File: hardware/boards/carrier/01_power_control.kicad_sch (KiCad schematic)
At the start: 15 parts, among them U1 STM32G031G6U6

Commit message: hardware: split carrier power controls and adopt SMBus
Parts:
- removed C11, C12: 100nF, Capacitor_SMD:C_0603_1608Metric, symbol Device:C
- removed C13: 4.7uF, Capacitor_SMD:C_0603_1608Metric, symbol Device:C
- removed LED1: WS2812B-2020-V6, LED_SMD:LED_WS2812B-2020_PLCC4_2.0x2.0mm, symbol LED:WS2812B-2020
- removed R24, R25, R26, R27: 2.2k, Resistor_SMD:R_0603_1608Metric, symbol Device:R
- removed R28: 10k, Resistor_SMD:R_0603_1608Metric, symbol Device:R
- removed R29: 100R, Resistor_SMD:R_0603_1608Metric, symbol Device:R
- removed TP1: SWDIO, TestPoint:TestPoint_Pad_D1.0mm, symbol Connector:TestPoint
- removed TP2: SWCLK, TestPoint:TestPoint_Pad_D1.0mm, symbol Connector:TestPoint
- removed TP3: NRST, TestPoint:TestPoint_Pad_D1.0mm, symbol Connector:TestPoint
- removed TP5: GND, TestPoint:TestPoint_Pad_D1.0mm, symbol Connector:TestPoint
- removed U1: STM32G031G6U6, Package_DFN_QFN:QFN-28_4x4mm_P0.5mm, symbol MCU_ST_STM32G0:STM32G031G6Ux
- added C1: 1uF 100V, Capacitor_SMD:C_1206_3216Metric, symbol Device:C
- added C10: 100nF, Capacitor_SMD:C_0603_1608Metric, symbol Device:C
- added C2: 680nF, Capacitor_SMD:C_0603_1608Metric, symbol Device:C
- added D1: SMCJ48A, Diode_SMD:D_SMC, symbol Device:D_Zener
- added MOD1: SW3538_140W_Module, mini-rack-power:SW3538_140W_Module, symbol mini-rack-power:SW3538_140W_Module
- added Q1: IPB020N10N5LF, Package_TO_SOT_SMD:TO-263-3_TabPin2, symbol Transistor_FET:Q_NMOS_GDS
- added Q2, Q3: 2N7002, Package_TO_SOT_SMD:SOT-23, symbol Transistor_FET:2N7002
- added R1: 6mR 1% 3W, Resistor_SMD:R_2512_6332Metric, symbol Device:R
- added R10: 100k, Resistor_SMD:R_0603_1608Metric, symbol Device:R
- added R11, R19: 10k, Resistor_SMD:R_0603_1608Metric, symbol Device:R
- added R17, R18: 10R, Resistor_SMD:R_0603_1608Metric, symbol Device:R
- added R2: 100R, Resistor_SMD:R_0603_1608Metric, symbol Device:R
- added R3: 36.0k 1%, Resistor_SMD:R_0603_1608Metric, symbol Device:R
- added R4, R6, R8: 110k 1%, Resistor_SMD:R_0603_1608Metric, symbol Device:R
- added R5: 18k 1%, Resistor_SMD:R_0603_1608Metric, symbol Device:R
- added R7: 5.1k 1%, Resistor_SMD:R_0603_1608Metric, symbol Device:R
- added R9: 36k 1%, Resistor_SMD:R_0603_1608Metric, symbol Device:R
- added U3: LMX5069MS, Package_SO:MSOP-10_3x3mm_P0.5mm, symbol Power_Management:LM5069MM-2
- added U4: INA237AIDGSR, Package_SO:TSSOP-10_3x3mm_P0.5mm, symbol Sensor_Energy:INA237
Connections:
- net +3V3: now also R11.1, R19.1, U4.6 (VS)
- net GND: now also C1.2, C2.2, D1.2 (A), MOD1.2 (GND), MOD1.4 (GND), Q2.2 (S), Q3.2 (S), R10.2, R3.2, R5.2, R7.2, R9.2, U3.5 (GND), U4.1 (A1), U4.2 (A0), U4.7 (GND)
- net INA_ALERT: now also R19.2, U4.3 (~{Alert})
- net PD_ENABLE: now also Q3.1 (G), R10.1
- net PD_I2C_SCL: now also MOD1.6 (SCL), U4.5 (SCL)
- net PD_I2C_SDA: now also MOD1.5 (SDA), U4.4 (SDA)
- net PD_PGOOD: now also R11.2, U3.8 (PGD)
- new net HS_OUT_SENSE: R2.1, U3.9 (OUT)
- new net HS_OVLO: R6.2, R7.1, U3.4 (OVLO)
- new net HS_PWR: R3.1, U3.7 (PWR)
- new net HS_SENSE: C1.1, Q1.2 (D), R1.2, R18.1, U3.1 (SENSE)
- new net HS_TIMER: C2.1, U3.6 (TIMER)
- new net HS_UVLO: Q2.3 (D), R4.2, R5.1, U3.3 (UVLO)
- new net INA_INM_FILT: C10.2, R18.2, U4.9 (Vin-)
- new net INA_INP_FILT: C10.1, R17.2, U4.10 (Vin+)
- new net KILL_GATE: Q2.1 (G), Q3.3 (D), R8.2, R9.1
- new net PD_VIN_SW: MOD1.1 (DC_IN), MOD1.3 (DC_IN), Q1.3 (S), R2.2, U4.8 (Vbus)
- new net Q1_GATE: Q1.1 (G), U3.10 (GATE)
- new net VCC: D1.1 (K), R1.1, R17.1, R4.1, R6.1, R8.1, U3.2 (VIN)
- no-connect marks 15 -> 1
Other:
- note added: "ASSEMBLY CHECK: verify U3/U4/Q1/MOD1 package pin numbering and footprints against manufacturer drawings."
- note added: "Default OFF: R8/R9 drive Q2 on unless PA1 drives Q3. LMX5069 auto-retries; STM32 observes PD_PGOOD and may remove PD_ENABLE."
- note added: "INA237 address fixed at 0x40: A0 = A1 = GND."
- note added: "POWER / CURRENT MONITOR"
- note added: "PROTECTED PD POWER + TELEMETRY + MODULE INTERFACE"
- note added: "Power path: VCC -> R1 (6 mR Kelvin-routed) -> HS_SENSE -> Q1 -> PD_VIN_SW"
- note added: "Q1 SOA RELEASE GATE Prove IPB020N10N5LF at the hot corner: approximately 66 W inferred maximum power limit and 66.5 ms maximum TIMER interval. Do not substitute Q1 using RDS(on) alone. Validate current/power limits and startup on hardware."
- note added: "R17/R18 are Kelvin sense traces from the R1 pads. U4 VBUS intentionally measures after Q1."
- note removed: "BUS PULL-UP OPTIONS"
- note removed: "MCU CORE / RESET / SWD"
- note removed: "R24/R25 are local PD-module I2C pull-ups. R26/R27 are backplane SMBus tuning options and are DNP when backplane pull-ups are fitted."
- note removed: "RGB STATUS LED"
- note removed: "STM32 HOUSEKEEPING, RESET, SWD, STATUS LED"
- title: USB-C PD Carrier - STM32 Housekeeping and Status -> USB-C PD Carrier - Protected Power and Controls

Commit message: checkpoint: carrier schematic edits and SW3538 references
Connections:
- net INA_INP_FILT: now also R17.1; no longer R17.2
- net VCC: now also R17.2; no longer R17.1
- net HS_OUT_SENSE: no longer names the net of R2.1, U3.9 (OUT)
- net HS_PWR: no longer names the net of R3.1, U3.7 (PWR)
- net HS_TIMER: no longer names the net of C2.1, U3.6 (TIMER)
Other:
- note added: "TODO: now that we have STM32, use the IRQ?"
- moved on the sheet: C1, C10, C2, D1, Q2, Q3, R1, R10, R11, R17, R18, R2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

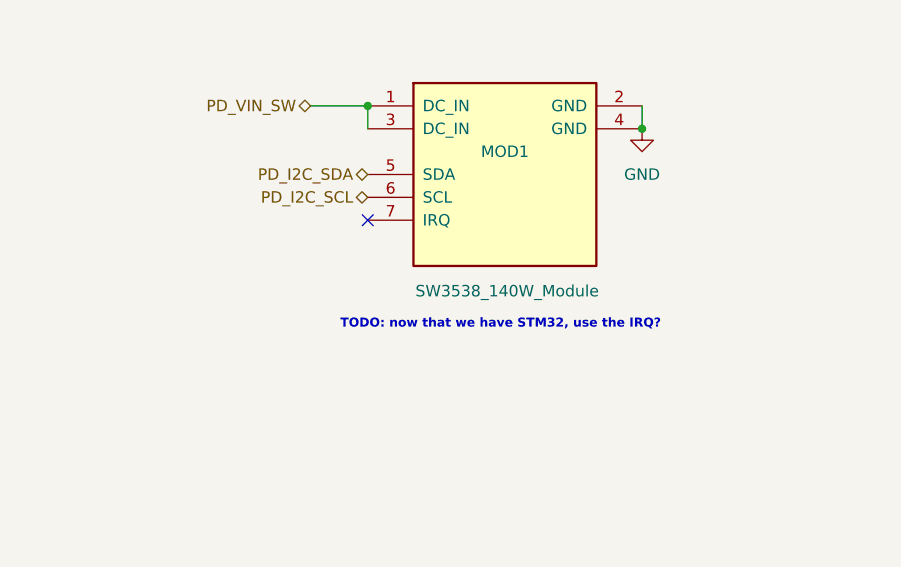
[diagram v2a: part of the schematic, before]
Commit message: hardware: route SW3538 IRQ to carrier MCU
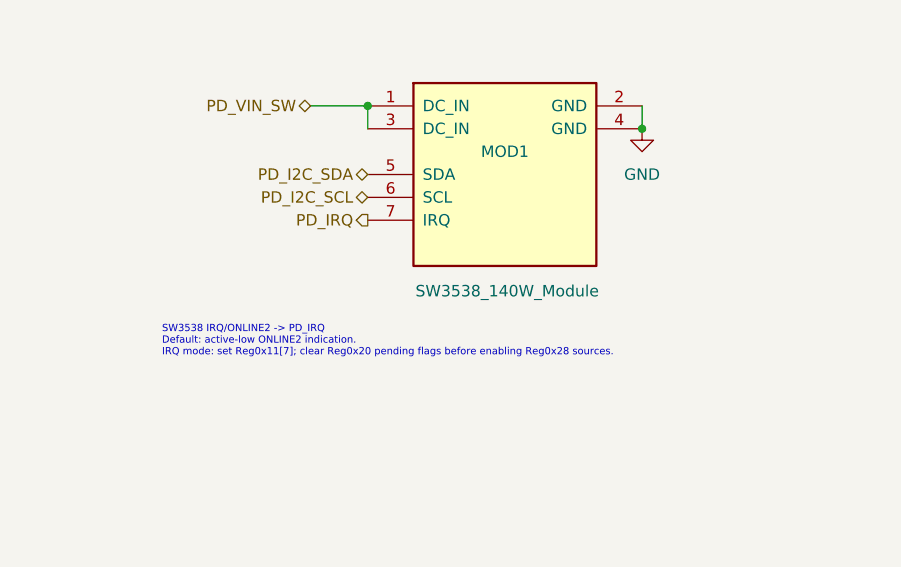
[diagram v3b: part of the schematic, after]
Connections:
- net PD_IRQ: now reaches MOD1.7 (IRQ)
- no-connect marks 1 -> 0
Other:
- note added: "SW3538 IRQ/ONLINE2 -> PD_IRQ Default: active-low ONLINE2 indication. IRQ mode: set Reg0x11[7]; clear Reg0x20 pending flags before enabling Reg0x28 sources."
- note removed: "TODO: now that we have STM32, use the IRQ?"
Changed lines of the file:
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@@
 		)
 	)
-	(text "TODO: now that we have STM32, use the IRQ?"
+	(text "SW3538 IRQ/ONLINE2 -> PD_IRQ\nDefault: active-low ONLINE2 indication.\nIRQ mode: set Reg0x11[7]; clear Reg0x20 pending flags before enabling Reg0x28 sources."
 		(exclude_from_sim no)
-		(at 355.092 62.992 0)
+		(at 335.28 66.04 0)
 		(effects
 			(font
-				(size 1 1)
-				(bold yes)
+				(size 0.8 0.8)
 			)
 			(justify left bottom)
@@
 		(color 0 0 0 0)
 	)
-	(no_connect
-		(at 358.14 50.8)
+	(hierarchical_label "PD_IRQ"
+		(shape output)
+		(at 358.14 50.8 180)
+		(effects
+			(font
+				(size 1.27 1.27)
+			)
+			(justify right bottom)
+		)
 	)
 	(wire

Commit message: checkpoint: carrier schematic readability edits
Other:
- moved on the sheet: R19
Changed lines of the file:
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@@
 	(text "Q1 SOA RELEASE GATE\nProve IPB020N10N5LF at the hot corner: approximately 66 W inferred maximum power limit and 66.5 ms maximum TIMER interval.\nDo not substitute Q1 using RDS(on) alone. Validate current/power limits and startup on hardware."
 		(exclude_from_sim no)
-		(at 292.1 94 0)
+		(at 179.578 16.002 0)
 		(effects
 			(font
@@
 	)
 	(junction
+		(at 265.43 137.16)
+		(diameter 0)
+		(color 0 0 0 0)
+	)
+	(junction
 		(at 264.16 35.56)
 		(diameter 0)
@@
 		(color 0 0 0 0)
 	)
-	(hierarchical_label "PD_IRQ"
-		(shape output)
-		(at 358.14 50.8 180)
-		(effects
-			(font
-				(size 1.27 1.27)
-			)
-			(justify right bottom)
-		)
-	)
 	(wire
 		(pts
@@
 	(wire
 		(pts
+			(xy 265.43 137.16) (xy 270.51 137.16)
+		)
+		(stroke
+			(width 0)
+			(type default)
+		)
+	)
+	(wire
+		(pts
 			(xy 251.46 40.64) (xy 256.54 40.64)
 		)
@@
 	(wire
 		(pts
+			(xy 248.92 137.16) (xy 265.43 137.16)
+		)
+		(stroke
+			(width 0)
+			(type default)
+		)
+	)
+	(wire
+		(pts
 			(xy 182.88 53.34) (xy 176.53 53.34)
 		)
@@
 	(wire
 		(pts
+			(xy 265.43 129.54) (xy 265.43 116.84)
+		)
+		(stroke
+			(width 0)
+			(type default)
+		)
+	)
+	(wire
+		(pts
 			(xy 289.56 35.56) (xy 280.67 35.56)
 		)
@@
 		)
 	)
+	(hierarchical_label "PD_IRQ"
+		(shape output)
+		(at 358.14 50.8 180)
+		(effects
+			(font
+				(size 1.27 1.27)
+			)
+			(justify right bottom)
+		)
+	)
 	(hierarchical_label "INA_ALERT"
 		(shape bidirectional)
-		(at 248.92 137.16 0)
+		(at 270.51 137.16 0)
 		(effects
 			(font
@@
 		)
 	)
-	(hierarchical_label "INA_ALERT"
-		(shape bidirectional)
-		(at 271.78 151.13 270)
-		(effects
-			(font
-				(size 1.27 1.27)
-			)
-			(justify right bottom)
-		)
-	)
 	(hierarchical_label "PD_I2C_SCL"
 		(shape bidirectional)
@@
 	(symbol
 		(lib_id "Device:R")
-		(at 271.78 147.32 0)
+		(at 265.43 133.35 0)
 		(unit 1)
 		(body_style 1)
@@
 		(dnp no)
 		(property "Reference" "R19"
-			(at 274.828 145.542 0)
+			(at 268.478 131.572 0)
 			(show_name no)
 			(do_not_autoplace no)
@@
 		)
 		(property "Value" "10k"
-			(at 275.082 149.352 0)
+			(at 268.732 135.382 0)
 			(show_name no)
 			(do_not_autoplace no)
@@
 		)
 		(property "Footprint" "Resistor_SMD:R_0603_1608Metric"
-			(at 270.002 147.32 90)
+			(at 263.652 133.35 90)
 			(hide yes)
 			(show_name no)
@@
 		)
 		(property "Datasheet" ""
-			(at 271.78 147.32 0)
+			(at 265.43 133.35 0)
 			(hide yes)
 			(show_name no)
@@
 		)
 		(property "Description" "Resistor"
-			(at 271.78 147.32 0)
+			(at 265.43 133.35 0)
 			(hide yes)
 			(show_name no)
@@
 	(symbol
 		(lib_id "power:+3V3")
-		(at 271.78 143.51 0)
+		(at 265.43 116.84 0)
 		(unit 1)
 		(body_style 1)
@@
 		(fields_autoplaced yes)
 		(property "Reference" "#PWR18"
-			(at 271.78 147.32 0)
+			(at 265.43 120.65 0)
 			(hide yes)
 			(show_name no)
@@
 		)
 		(property "Value" "+3V3"
-			(at 271.78 138.43 0)
+			(at 265.43 111.76 0)
 			(show_name no)
 			(do_not_autoplace no)
@@
 		)
 		(property "Footprint" ""
-			(at 271.78 143.51 0)
+			(at 265.43 116.84 0)
 			(hide yes)
 			(show_name no)
@@
 		)
 		(property "Datasheet" ""
-			(at 271.78 143.51 0)
+			(at 265.43 116.84 0)
 			(hide yes)
 			(show_name no)
@@
 		)
 		(property "Description" "Power symbol creates a global label with name \"+3V3\""
-			(at 271.78 143.51 0)
+			(at 265.43 116.84 0)
 			(hide yes)
 			(show_name no)

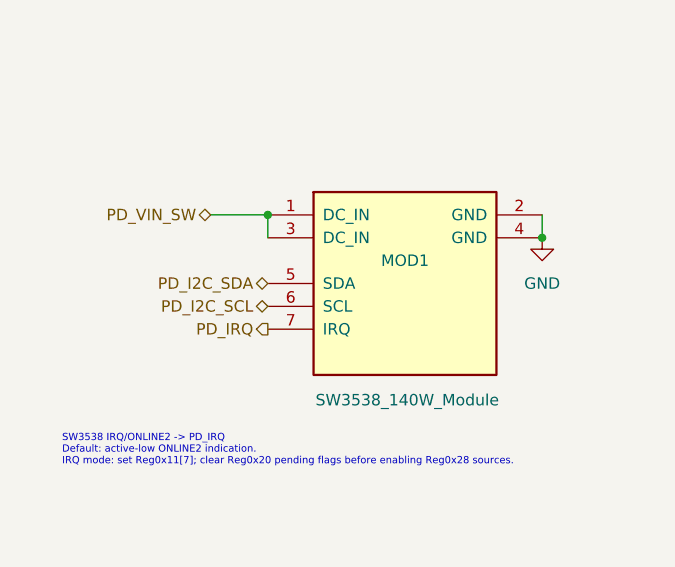
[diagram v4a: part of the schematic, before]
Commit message: hardware: prepare carrier mechanics and assembly
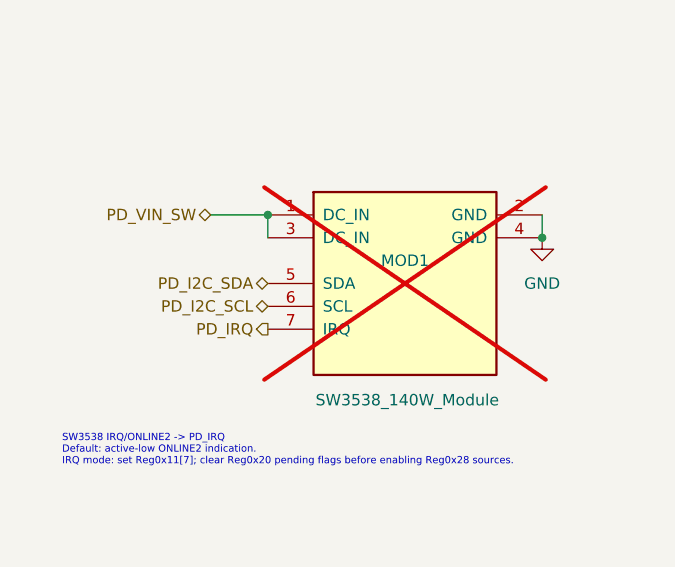
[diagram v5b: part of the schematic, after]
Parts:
- MOD1: now not fitted
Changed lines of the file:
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@@
 		(in_bom yes)
 		(on_board yes)
-		(in_pos_files yes)
-		(dnp no)
+		(in_pos_files no)
+		(dnp yes)
 		(property "Reference" "MOD1"
 			(at 373.38 43.18 0)

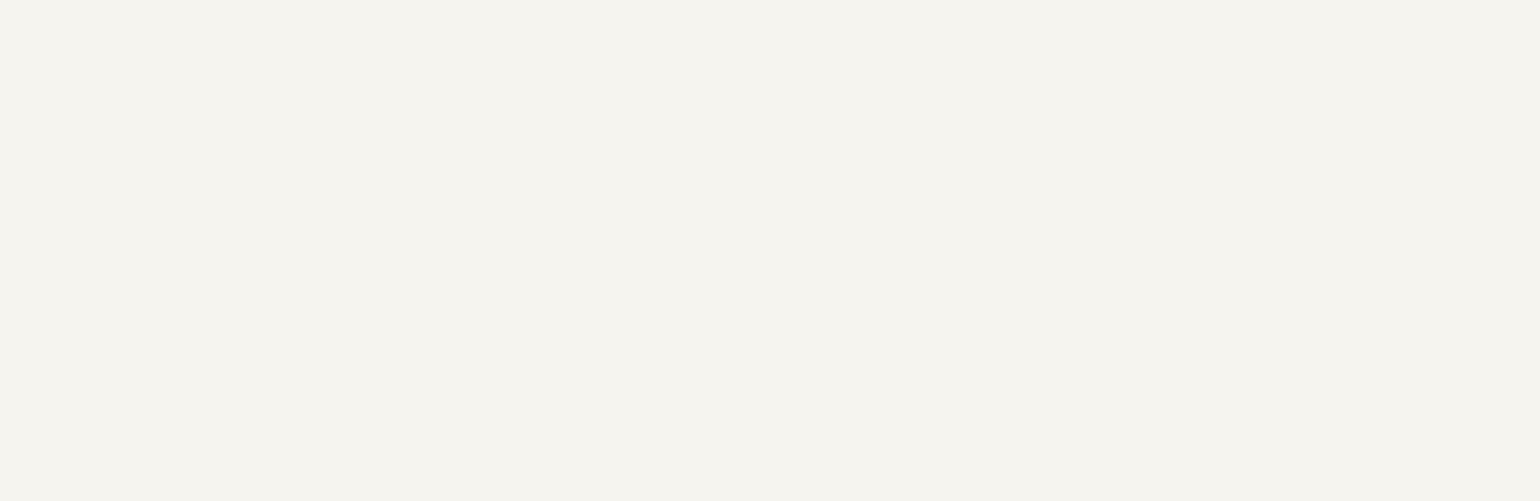
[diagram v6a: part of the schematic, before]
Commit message: Replace carrier backplane SMBus with CAN-FD
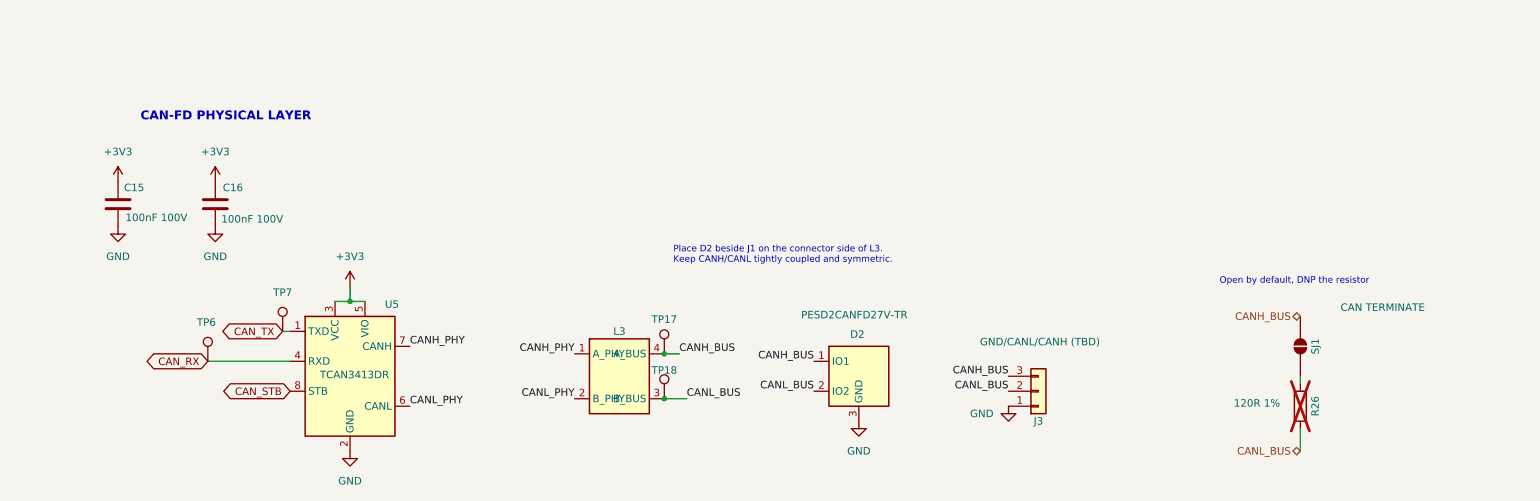
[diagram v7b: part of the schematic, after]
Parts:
- added C15, C16: 100nF 100V, Capacitor_SMD:C_0603_1608Metric, symbol Device:C
- added D2: PESD2CANFD27V-TR, Package_TO_SOT_SMD:SOT-23, symbol backplane-backpack:PESD_Dual_SOT23
- added J3: GND/CANL/CANH (TBD), symbol Connector_Generic:Conn_01x03
- added L3: ACT1210D-101-2P-TL00, symbol backplane-backpack:ACT1210D_1243
- added R26: 120R 1%, Resistor_SMD:R_0603_1608Metric, symbol Device:R
- added SJ1: CAN TERMINATE, Jumper:SolderJumper-2_P1.3mm_Open_Pad1.0x1.5mm, symbol Jumper:SolderJumper_2_Open
- added TP17: CANH_BUS, TestPoint:TestPoint_Pad_D1.5mm, symbol Connector:TestPoint
- added TP18: CANL_BUS, TestPoint:TestPoint_Pad_D1.5mm, symbol Connector:TestPoint
- added TP6: CAN_RX, TestPoint:TestPoint_Pad_D1.5mm, symbol Connector:TestPoint
- added TP7: CAN_TX, TestPoint:TestPoint_Pad_D1.5mm, symbol Connector:TestPoint
- added U5: TCAN3413DR, Package_SO:SOIC-8_3.9x4.9mm_P1.27mm, symbol backplane-backpack:TCAN3413DR
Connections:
- net +3V3: now also C15.1, C16.1, U5.3 (VCC), U5.5 (VIO)
- net GND: now also C15.2, C16.2, D2.3 (GND), J3.1 (Pin_1), U5.2 (GND)
- new net: R26.1, SJ1.2 (B)
- new net CANH_BUS: D2.1 (IO1), J3.3 (Pin_3), L3.4 (A_BUS), SJ1.1 (A), TP17.1
- new net CANH_PHY: L3.1 (A_PHY), U5.7 (CANH)
- new net CANL_BUS: D2.2 (IO2), J3.2 (Pin_2), L3.3 (B_BUS), R26.2, TP18.1
- new net CANL_PHY: L3.2 (B_PHY), U5.6 (CANL)
- new net CAN_RX: TP6.1, U5.4 (RXD)
- new net CAN_STB: U5.8 (STB)
- new net CAN_TX: TP7.1, U5.1 (TXD)
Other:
- note added: "CAN-FD PHYSICAL LAYER"
- note added: "Open by default, DNP the resistor"
- note added: "Place D2 beside J1 on the connector side of L3. Keep CANH/CANL tightly coupled and symmetric."
